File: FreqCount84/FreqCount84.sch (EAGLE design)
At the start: 46 parts, among them IC1 74LS595D, IC2 74LS595D, IC3 74LS595D, IC4 74S151D, IC5 7805T, Q1 20.000MHz

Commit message: FreqCount84 adding Input Stage (AC / DC coupling and Amplification); updated resistor and capacitor libraries so that the values and names are on the same side of the symbol rather than opposite sides
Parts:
- added C3, C4: 0.1u, rcl:C-EUC0603
- added D1, D2, D3: 1N4004, diode:1N4004
- added FREQ-INPUT: I/O, !synth_sch:MONO_JACK
- added IC6: 74AHCU04, 74xx-us:74ALS04D
- added R2: 1, rcl:R-US_R0603
- added R21, R24: 1M, rcl:R-US_R0603
- added R22, R23: 1k, rcl:R-US_R0603
- added R25: 10k, rcl:R-US_R0603
- added R3: 100k, rcl:R-US_R0603
- added S1: PVA2R, switch-misc:PVA2R
- added T1: 2N3904, transistor:2N3904
- added U$8: 2N7000, !synth_sch:2N7000
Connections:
- removed net FREQ-IN: IC4A.D0, V11.CLK
- new net FREQ-AC-COUPLED: IC6F.O, S12.O
- new net FREQ-DC-COUPLED: R23.2, R24.1, S12.S, U$8.D
- new net FREQ-DIGITAL-IN: IC4A.D0, S12.P, V11.CLK
- new net N$22: IC6A.O, IC6B.I, R3.2
- new net N$23: IC6C.O, IC6D.I
- new net N$42: IC6D.O, IC6E.I
- new net N$43: IC6E.O, IC6F.I
- new net N$44: IC6B.O, IC6C.I
- new net N$45: C3.1, IC6P.VCC, R2.1
- new net N$46: R22.2, T1.C, U$8.G
- new net N$47: C4.1, S11.O
- new net N$49: R25.2, S11.S
- new net N$50: FREQ-INPUT.P2, S11.P
- new net N$52: C4.2, D2.C, D3.A, IC6A.I, R21.1, R3.1
- new net N$54: D1.C, R24.2, R25.1, T1.B
- net +5V: now also D3.C, R2.2, R22.1, R23.1
- net GND: now also C3.2, D1.A, D2.A, FREQ-INPUT.P$1, FREQ-INPUT.P3, IC6P.GND, R21.2, T1.E, U$8.S
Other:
- note added: "Switch Position 1: AC Coupling This signal path will amplify and digitize the signal (clip the signal to 0 or 5 V). This is intended to work for high frequency signals. The input impedance should be around 91 kΩ for frequencies where the reactance of the input cap and the logic gate's capacitance are negligible. The lower bound is determined by the time of the input AC-coupling filter (time const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"
- note added: "Switch Position 2: DC Coupling This signal path will amplify and digitize the signal (clip the signal to 0 or 5 V). This is inteded to work for an arbitrarily low frequenciesl. You could measure things that take decades with this path."

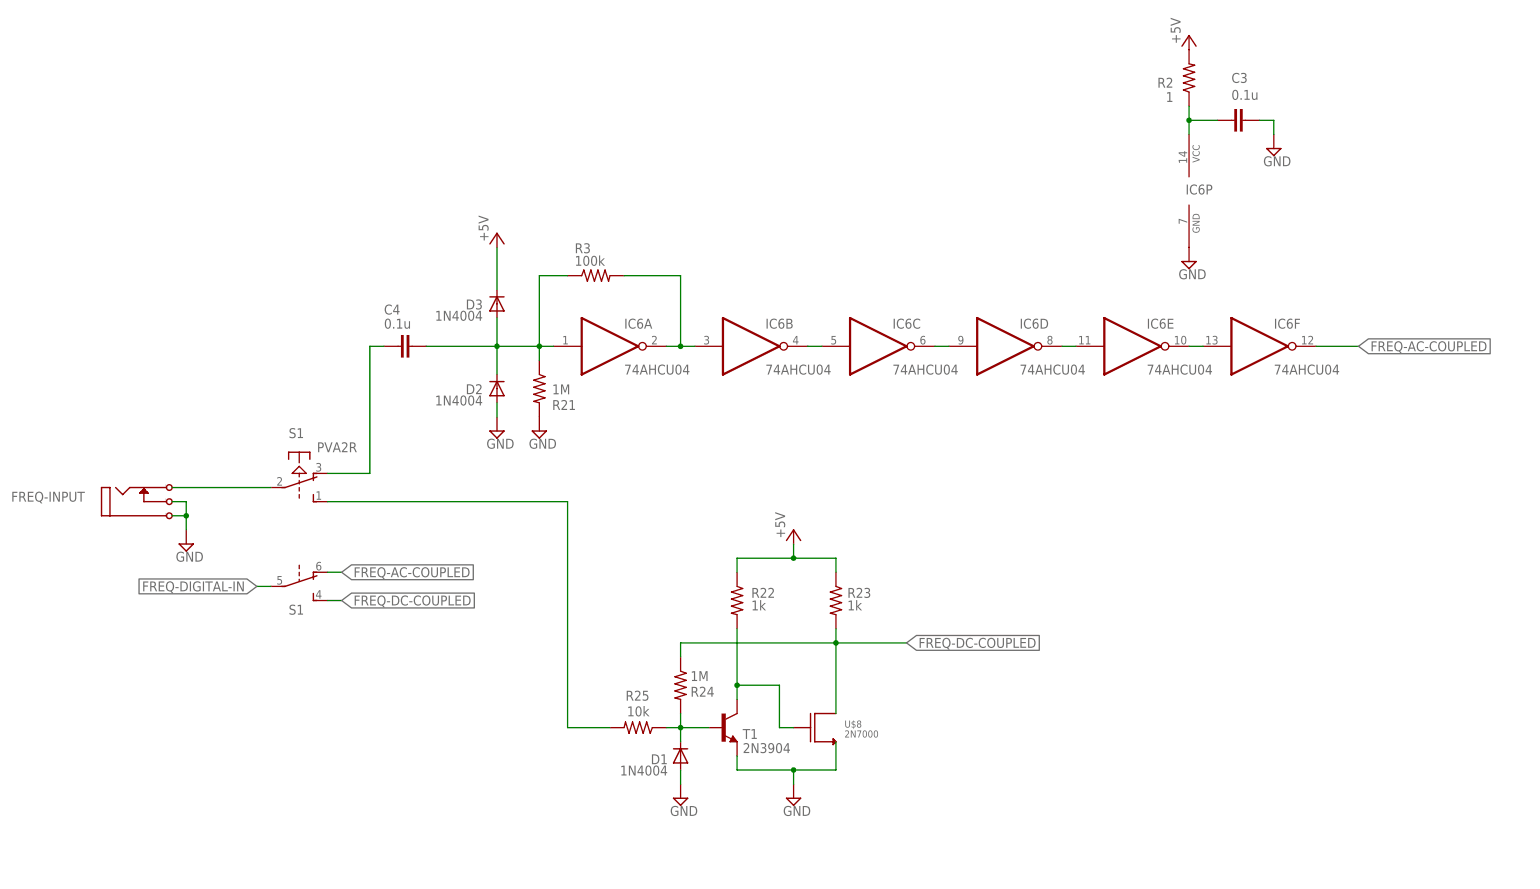
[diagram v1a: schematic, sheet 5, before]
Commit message: added the FTDI USB->RS232 chip into the schematic because I am using it now.
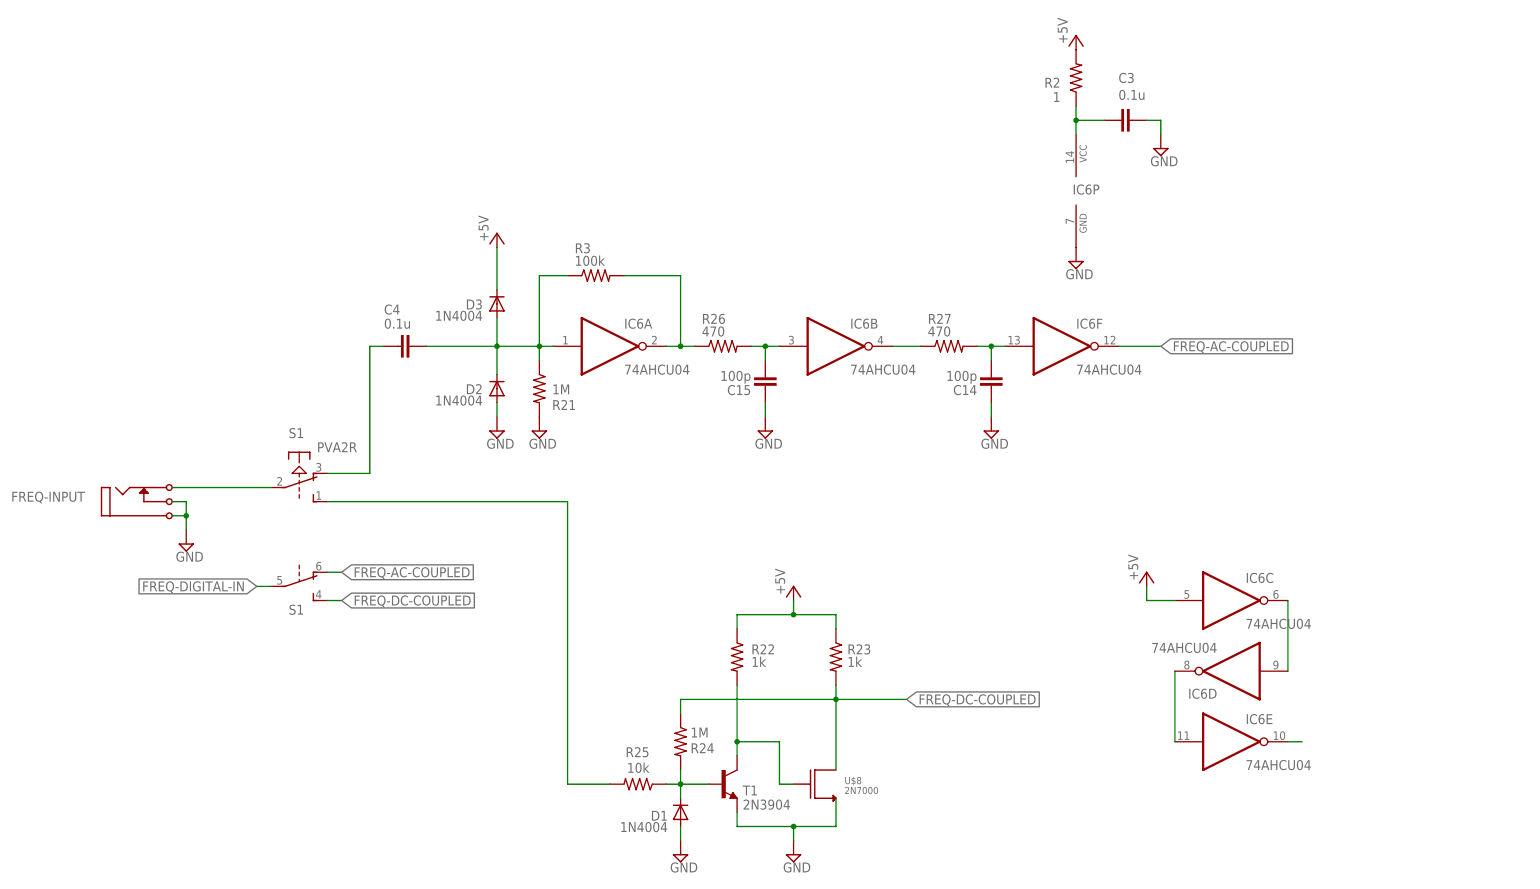
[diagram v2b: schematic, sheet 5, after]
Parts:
- added C14, C15: 100p, rcl:C-EUC0603
- added IC7: FT232RL, ftdichip:FT232RL
- added R26, R27: 470, rcl:R-US_R0603
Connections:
- removed net N$44 (its old number): IC6B.O, IC6C.I
- new net N$23: C15.2, IC6B.I, R26.2
- new net N$42: C14.2, IC6F.I, R27.2
- new net N$51: IC6E.O
- new net N$53: IC7.TXD, U$1.P$13
- new net N$58: IC7.USBDP
- new net N$59: IC7.USBDM
- new net N$60: IC7.VCC
- net +5V: now also IC6C.I
- net GND: now also C14.1, C15.1, IC7.GND, IC7.GND@1, IC7.GND@2, IC7.GND@A
- net N$22: now also R26.1; no longer IC6B.I
- net N$43: now also IC6B.O, R27.1; no longer IC6E.O, IC6F.I
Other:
- note added: "USB connector"
- note added: "Unused gates from the hex inverter chip"
- moved on the sheet: C1, C11, C3, D1, IC5, IC6B, IC6C, IC6D, IC6E, IC6F, IC6P, JP1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

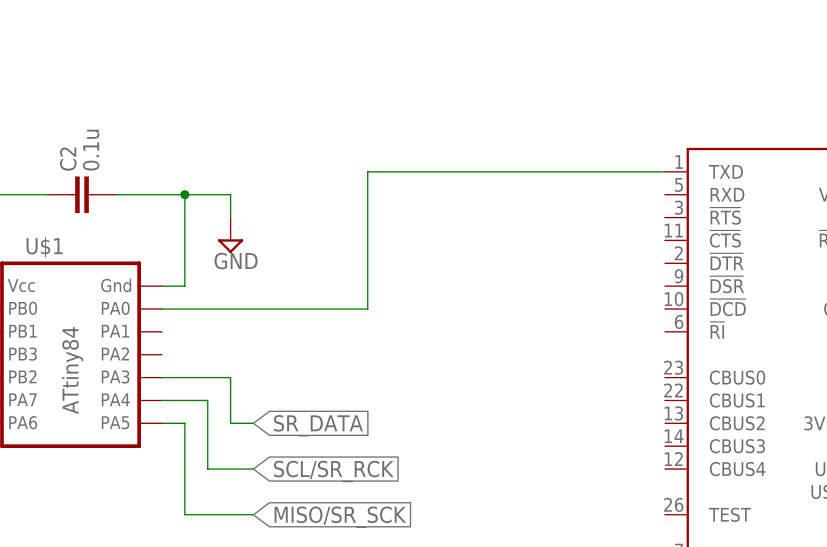
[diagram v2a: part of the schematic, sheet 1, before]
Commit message: adding notes to FTDI RS232 chip.
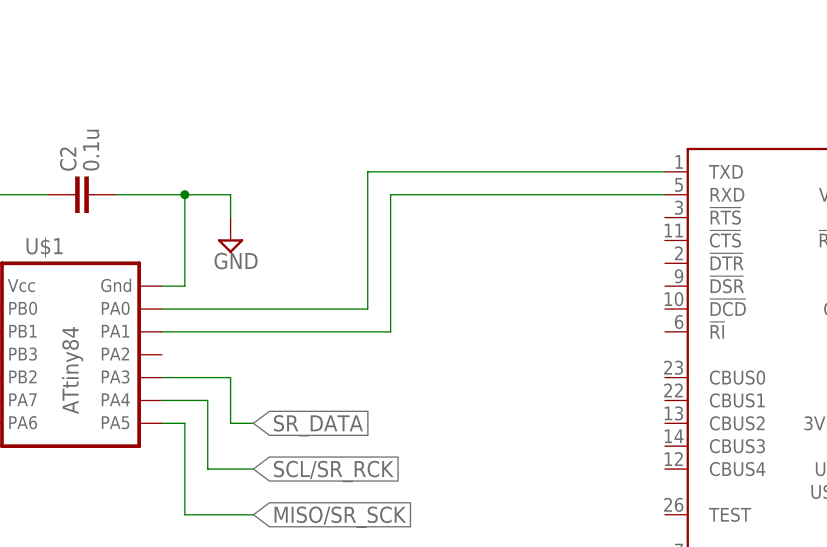
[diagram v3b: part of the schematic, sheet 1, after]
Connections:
- new net N$55: IC7.RXD, U$1.P$12
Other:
- note added: "USB->Serial UART (RS232) chip This is optional. Populate this chip if you want to be able to automatically record measurements using a computer"
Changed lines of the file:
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@@
 <text x="-15.24" y="134.62" size="2.54" layer="98" align="center">A frequency counter designed around the ATtiny84</text>
 <text x="111.76" y="71.12" size="1.778" layer="98">USB connector</text>
+<text x="45.72" y="114.3" size="1.778" layer="98">USB-&gt;Serial UART (RS232) chip
+This is optional. Populate this chip if you want to be able
+to automatically record measurements using a computer</text>
 </plain>
 <instances>
@@
 </segment>
 </net>
+<net name="N$55" class="0">
+<segment>
+<pinref part="IC7" gate="1" pin="RXD"/>
+<wire x1="60.96" y1="104.14" x2="30.48" y2="104.14" width="0.1524" layer="91"/>
+<wire x1="30.48" y1="104.14" x2="30.48" y2="88.9" width="0.1524" layer="91"/>
+<pinref part="U$1" gate="G$1" pin="P$12"/>
+<wire x1="30.48" y1="88.9" x2="5.08" y2="88.9" width="0.1524" layer="91"/>
+</segment>
+</net>
